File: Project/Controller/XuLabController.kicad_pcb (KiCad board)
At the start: 4 copper layers, 75 x 81 mm, 94 parts, among them J1 Power, J10 Servo, J11 Servo, J12 Servo, J13 Thruster, J14 I2C, J15 I2C, J16 UART1, J17 UART2, J18 SPI1, J19 SPI2, J2 SWD, J20 Interrupt, J21 Interrupt, J22 Interrupt, J3 USB_C_Receptacle_USB2.0_16P, J4 Bar30, J5 Servo, J6 Servo, J7 Servo, J8 Servo, J9 Servo, SW1 SW_SPDT, SW2 SW_SPDT, SW3 SW_Push, U1 LM66100DCK, U10 SHTC3, U2 MIC5219-3.3YM5, U3 LM66100DCK, U4 STM32F446RCTx, U5 24AA64-OT, U6 USBLC6-2SC6, U7 BMI088, U8 MMC5983MA, U9 MCP9700Ax-ETT, Y1 8MHz

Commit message: Add client credits
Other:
- board text added: "Clients: Matticus Brown Marshall Graybill Nicole Xu"
- board text added: "Designed By: Owen Allison 03/2026 - Rev B"
- board text removed: "3.3 V"
- board text removed: "Designed By: Owen Allison"
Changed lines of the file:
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@@
+		)
+	)
+	(gr_text "GND"
+		(at 129.25 132.25 0)
+		(layer "F.SilkS")
+		(effects
+			(font
+				(size 1 1)
+				(thickness 0.15)
+			)
+			(justify bottom)
 		)
 	)
@@
 		)
 	)
-	(gr_text "3.3 V"
-		(at 126 132.5 0)
-		(layer "F.SilkS")
-		(effects
-			(font
-				(size 1 1)
-				(thickness 0.15)
-			)
-			(justify left bottom)
+	(gr_text "3V3"
+		(at 126.75 128.5 0)
+		(layer "F.SilkS")
+		(effects
+			(font
+				(size 1 1)
+				(thickness 0.15)
+			)
+			(justify bottom)
 		)
 	)
@@
 		)
 	)
-	(gr_text "Designed By: Owen Allison"
-		(at 173 73.25 0)
+	(gr_text "Designed By: Owen Allison\n03/2026 - Rev B"
+		(at 173 70.5 0)
 		(layer "B.SilkS")
 		(effects
@@
 				(thickness 0.15)
 			)
-			(justify left bottom mirror)
-		)
-	)
+			(justify left top mirror)
+		)
+	)
+	(gr_text "Clients:\nMatticus Brown\n\nMarshall Graybill\n\nNicole Xu"
+		(at 135.25 107.75 0)
+		(layer "B.SilkS")
+		(effects
+			(font
+				(size 1 1)
+				(thickness 0.15)
+			)
+			(justify left top mirror)
+		)
+	)

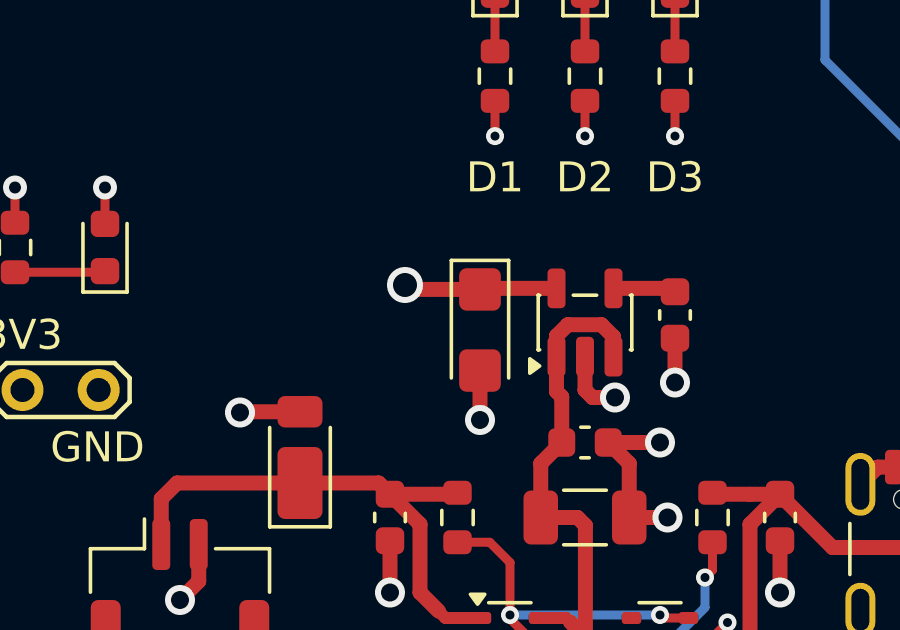
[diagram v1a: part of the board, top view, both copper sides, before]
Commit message: Add more power input vias
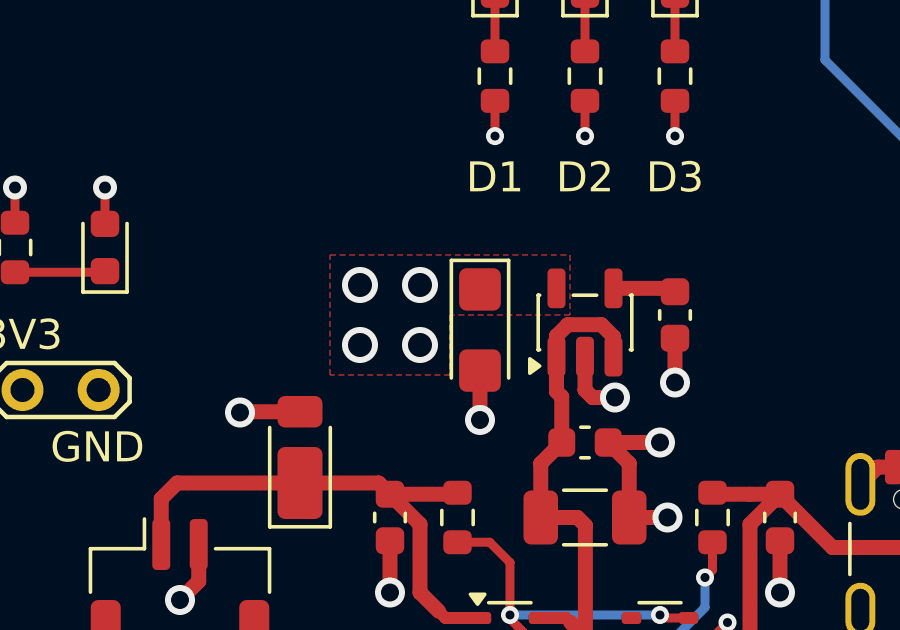
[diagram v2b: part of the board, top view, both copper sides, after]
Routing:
- net +3.3V: track 82.4 -> 77.5 mm, vias 26 -> 29
- added copper zone on F.Cu, net +3.3V
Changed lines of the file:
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@@
 	)
 	(segment
-		(start 139.6475 126.3975)
-		(end 139.5 126.25)
-		(width 0.5)
-		(layer "F.Cu")
-		(net 5)
-	)
-	(segment
 		(start 156.125 63.125)
 		(end 155.75 62.75)
@@
 	)
 	(segment
-		(start 144.55 126.3625)
-		(end 142.215 126.3625)
-		(width 0.5)
-		(layer "F.Cu")
-		(net 5)
-	)
-	(segment
 		(start 168.625 63.125)
 		(end 168.25 62.75)
@@
 	)
 	(segment
-		(start 142 126.3975)
-		(end 139.6475 126.3975)
-		(width 0.5)
-		(layer "F.Cu")
-		(net 5)
-	)
-	(segment
 		(start 163.425 75.25)
 		(end 163.425 76.85)
@@
 	)
 	(via
+		(at 138 128.25)
+		(size 1.2)
+		(drill 0.8)
+		(layers "F.Cu" "B.Cu")
+		(free yes)
+		(net 5)
+	)
+	(via
 		(at 112.25 67.5)
 		(size 0.8)
@@
 	)
 	(via
-		(at 139.5 126.25)
+		(at 140 126.25)
+		(size 1.2)
+		(drill 0.8)
+		(layers "F.Cu" "B.Cu")
+		(free yes)
+		(net 5)
+	)
+	(via
+		(at 138 126.25)
 		(size 1.2)
 		(drill 0.8)
@@
 	)
 	(via
+		(at 140 128.25)
+		(size 1.2)
+		(drill 0.8)
+		(layers "F.Cu" "B.Cu")
+		(free yes)
+		(net 5)
+	)
+	(via
 		(at 153.25 83.5)
 		(size 0.6)
@@
 	)
 	(zone
+		(net 5)
+		(net_name "+3.3V")
+		(layer "F.Cu")
+		(hatch edge 0.5)
+		(priority 4)
+		(connect_pads yes
+			(clearance 0.2)
+		)
+		(min_thickness 0.25)
+		(filled_areas_thickness no)
+		(fill yes
+			(thermal_gap 0.5)
+			(thermal_bridge_width 0.5)
+		)
+		(polygon
+			(pts
+				(xy 137 125.25) (xy 145 125.25) (xy 145 127.25) (xy 141 127.25) (xy 141 129.25) (xy 137 129.25)
+			)
+		)
+	)
+	(zone

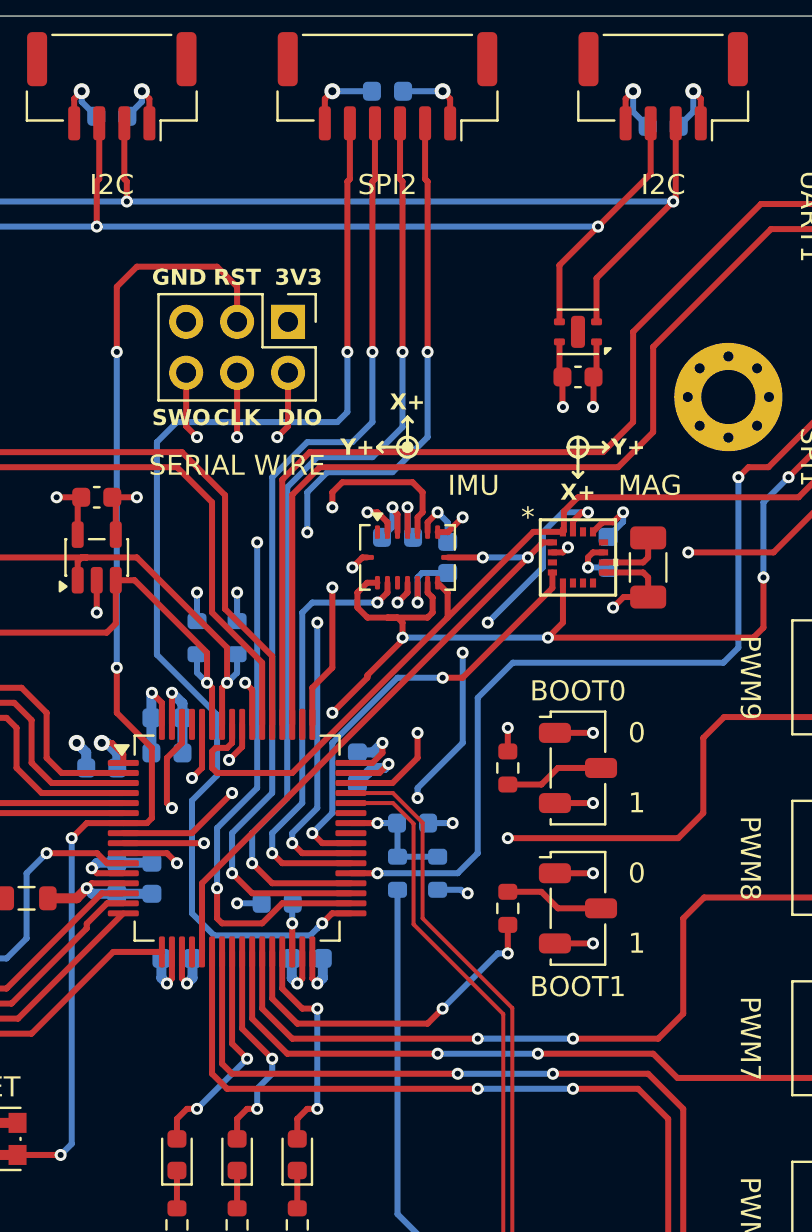
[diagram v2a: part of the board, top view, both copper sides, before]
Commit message: Change IMU to BMI330
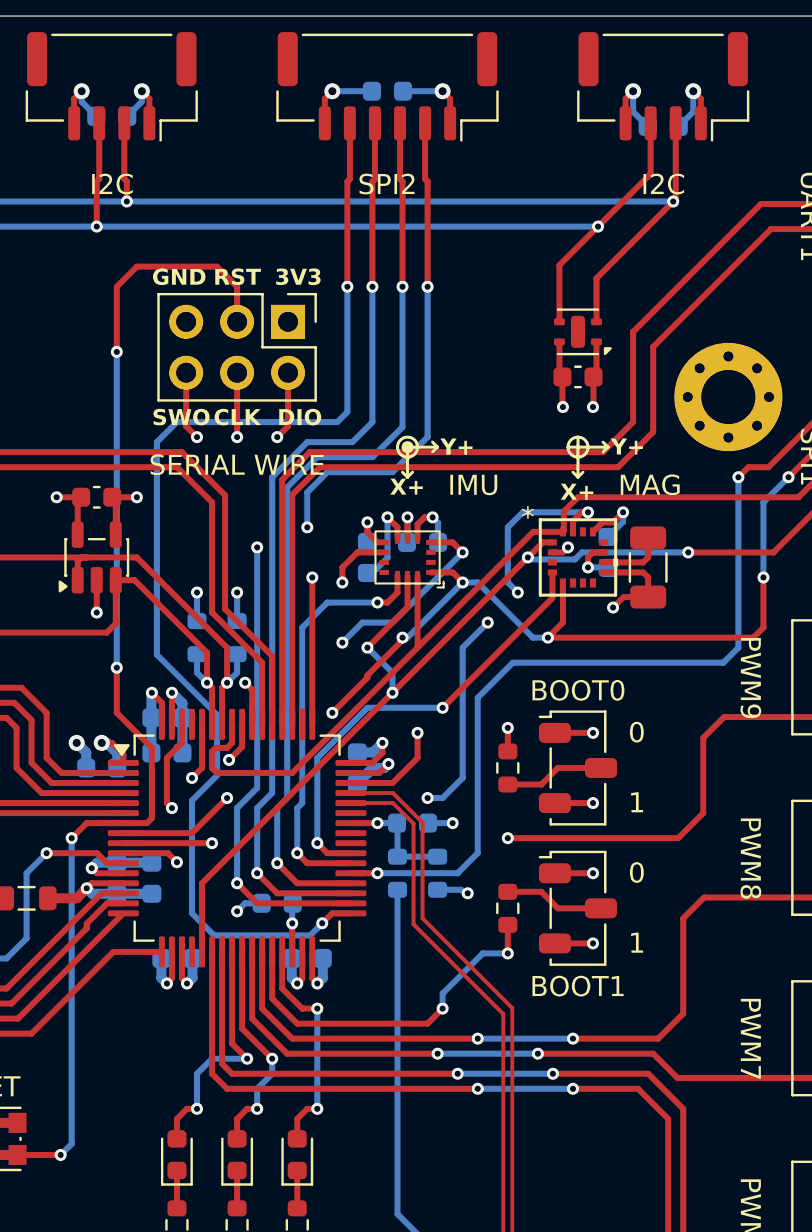
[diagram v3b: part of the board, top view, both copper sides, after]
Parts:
- U7: value BMI088 -> BMI330; footprint Package_LGA:Bosch_LGA-16_4.5x3mm_P0.5mm_LayoutBorder7x1y_ClockwisePinNumbering -> XuLab:BMI330
- moved C21 1.80 mm to (152.0, 86.0), turned to -90 degrees
- moved C22 1.46 mm to (154.8, 85.2), turned to 180 degrees
- turned U7 to 180 degrees
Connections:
- U4 pad 40: /SPI1_CS3 -> /Microcontroller/SPI1_CS3
- U7 pad 1: /Sensors/ACCL_INT2 -> /SPI1_MISO
- U7 pad 10: /SPI1_MISO -> unconnected-(U7-NC-Pad10)
- U7 pad 11: +3.3V -> unconnected-(U7-NC-Pad11)
- U7 pad 12: /GPIO_EXTI1 -> /SPI1_CS1
- U7 pad 13: /Sensors/GYRO_INT2 -> /SPI1_SCK
- U7 pad 14: /SPI1_CS1 -> /SPI1_MOSI
- U7 pad 2: GND -> unconnected-(U7-NC-Pad2)
- U7 pad 3: +3.3V -> unconnected-(U7-NC-Pad3)
- U7 pad 4: GND -> /GPIO_EXTI1
- U7 pad 5: /SPI1_CS2 -> +3.3V
- U7 pad 8: /SPI1_SCK -> +3.3V
- U7 pad 9: /SPI1_MOSI -> /GPIO_EXTI0
- U8 pad 4: /SPI1_CS3 -> /SPI1_CS2
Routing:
- net /SPI1_CS3: track 22.0 -> 0.00 mm, vias 2 -> 0
- net /SPI1_CS2: track 28.5 -> 22.4 mm, vias 3 -> 2
- net /SPI1_MISO: track 57.1 -> 51.9 mm, vias 6 -> 7
- net /GPIO_EXTI1: track 22.8 -> 26.8 mm, vias 2 -> 3
- net /SPI2_SCK: track 54.3 -> 51.1 mm
- net /SPI1_SCK: track 50.4 -> 53.6 mm, vias 3 -> 4
- net GND: track 128.2 -> 126.3 mm, vias 49 -> 47
- net /SPI2_MOSI: track 47.0 -> 45.2 mm
- net /SPI2_MISO: track 48.0 -> 46.2 mm
- net /GPIO_EXTI2: track 40.2 -> 38.5 mm
- net /Microcontroller/SW_CLK: track 20.8 -> 19.1 mm
- net /SPI1_MOSI: track 44.7 -> 46.3 mm
- net +3.3V: track 77.5 -> 76.1 mm
- net /SPI1_CS1: track 21.9 -> 20.5 mm
- net /Microcontroller/SW_DIO: track 29.5 -> 28.4 mm
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
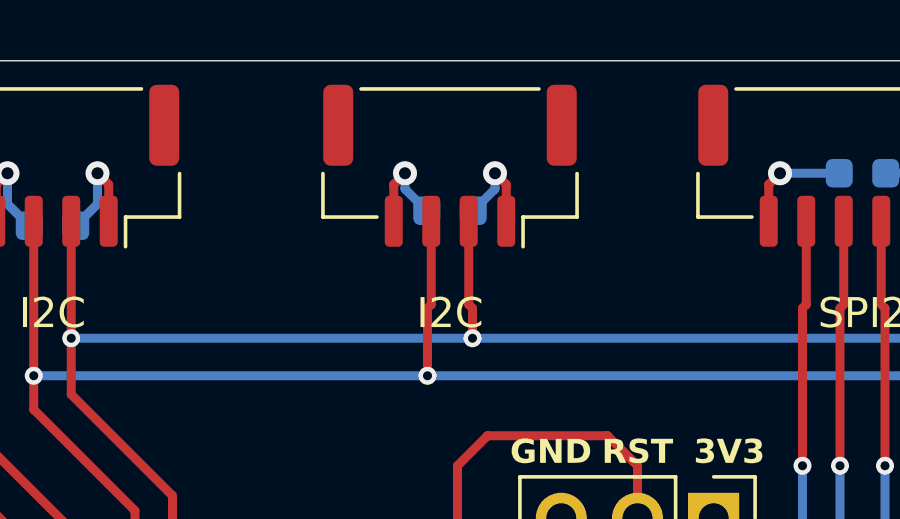
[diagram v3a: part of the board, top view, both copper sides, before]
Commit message: Fix connector capacitor alignment
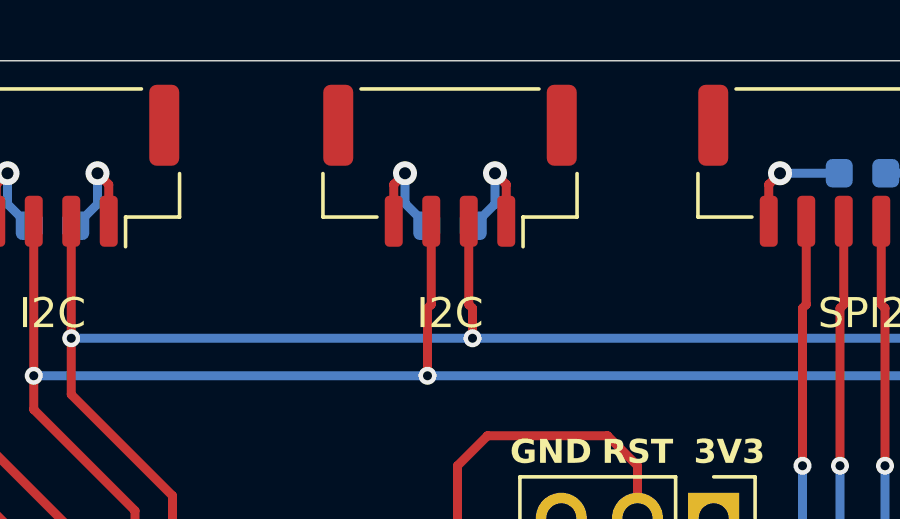
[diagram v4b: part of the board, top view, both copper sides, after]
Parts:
- moved C23 0.50 mm to (139.2, 64.5)
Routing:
- net GND: track 126.3 -> 126.8 mm
- net +3.3V: track 76.1 -> 76.6 mm
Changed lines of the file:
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@@
 	(footprint "Capacitor_SMD:C_0603_1608Metric"
 		(layer "B.Cu")
-		(at 139.25 64 180)
+		(at 139.25 64.5 180)
 		(descr "Capacitor SMD 0603 (1608 Metric), square (rectangular) end terminal, IPC-7351 nominal, (Body size source: IPC-SM-782 page 76, https://www.pcb-3d.com/wordpress/wp-content/uploads/ipc-sm-782a_amendment_1_and_2.pdf), generated with kicad-footprint-generator")
 		(tags "capacitor")
@@
 	)
 	(segment
+		(start 138.475 64.475)
+		(end 138.475 64.5)
+		(width 0.3)
+		(layer "B.Cu")
+		(net 2)
+	)
+	(segment
 		(start 112.25 70.5)
 		(end 113.275 70.5)
@@
 	)
 	(segment
+		(start 137.75 62.75)
+		(end 137.75 63.75)
+		(width 0.3)
+		(layer "B.Cu")
+		(net 2)
+	)
+	(segment
 		(start 153 86.025)
 		(end 152.25 86.775)
@@
 	)
 	(segment
-		(start 161.075 133.825)
-		(end 161.5 134.25)
+		(start 137.75 63.75)
+		(end 138.475 64.475)
 		(width 0.3)
 		(layer "B.Cu")
@@
 	)
 	(segment
-		(start 137.75 62.75)
-		(end 137.75 63.275)
+		(start 161.075 133.825)
+		(end 161.5 134.25)
 		(width 0.3)
 		(layer "B.Cu")
@@
 	)
 	(segment
-		(start 137.75 63.275)
-		(end 138.475 64)
-		(width 0.3)
-		(layer "B.Cu")
-		(net 2)
-	)
-	(segment
 		(start 128.0625 105.6875)
 		(end 127.5 106.25)
@@
 	)
 	(segment
-		(start 140.75 62.75)
-		(end 140.75 63.275)
-		(width 0.3)
-		(layer "B.Cu")
-		(net 5)
-	)
-	(segment
 		(start 139.525 95.775)
 		(end 139 95.25)
@@
 	)
 	(segment
+		(start 140.75 62.75)
+		(end 140.75 63.775)
+		(width 0.3)
+		(layer "B.Cu")
+		(net 5)
+	)
+	(segment
 		(start 149.775 106.975)
 		(end 149.5 107.25)
@@
 	)
 	(segment
+		(start 140.75 63.775)
+		(end 140.025 64.5)
+		(width 0.3)
+		(layer "B.Cu")
+		(net 5)
+	)
+	(segment
 		(start 143.25 106.025)
 		(end 143.275 106)
@@
 		(layer "B.Cu")
 		(net 5)
-	)
-	(segment
-		(start 140.75 63.275)
-		(end 140.025 64)
-		(width 0.3)
-		(layer "B.Cu")
-		(net 5)
